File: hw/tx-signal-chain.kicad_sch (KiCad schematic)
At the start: 29 parts, among them J501 Conn_Coaxial_Power, K501 TQ2-5V, Q501 IRFP250NPBF, Q502 2N7002AKRA-QZ, T501 1t (coax center feedthru) : 8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, U501 UCC27511ADBV

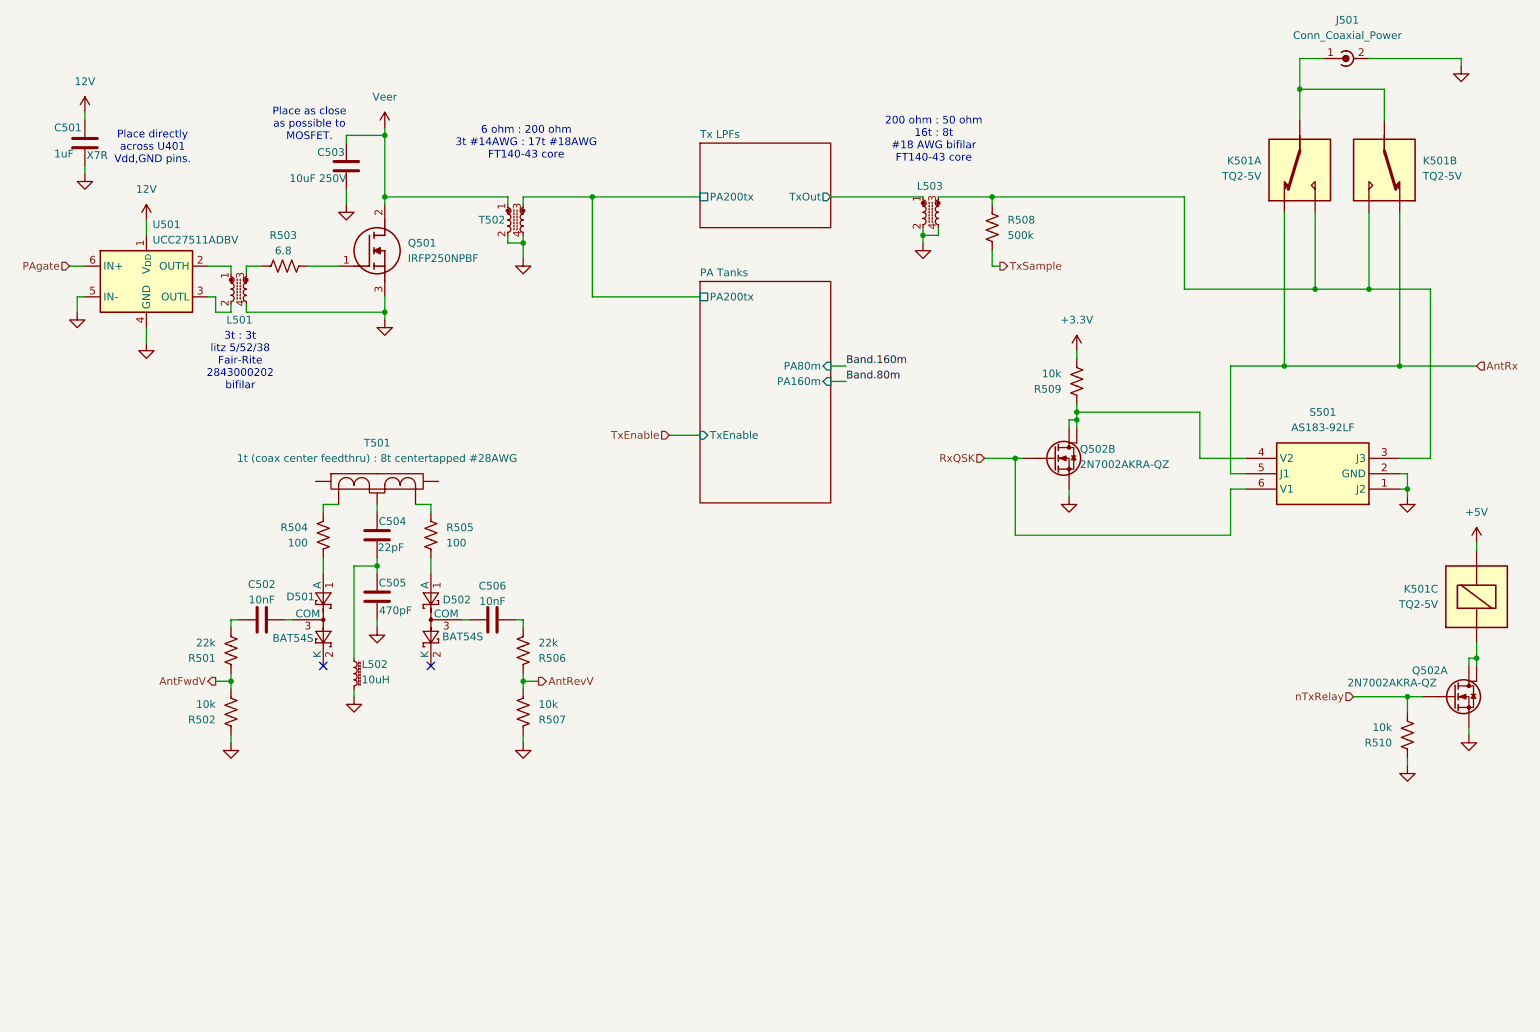
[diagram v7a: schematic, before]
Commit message: Removed USB data, SD card. Added USB-PD (not complete yet). Added SPI display.
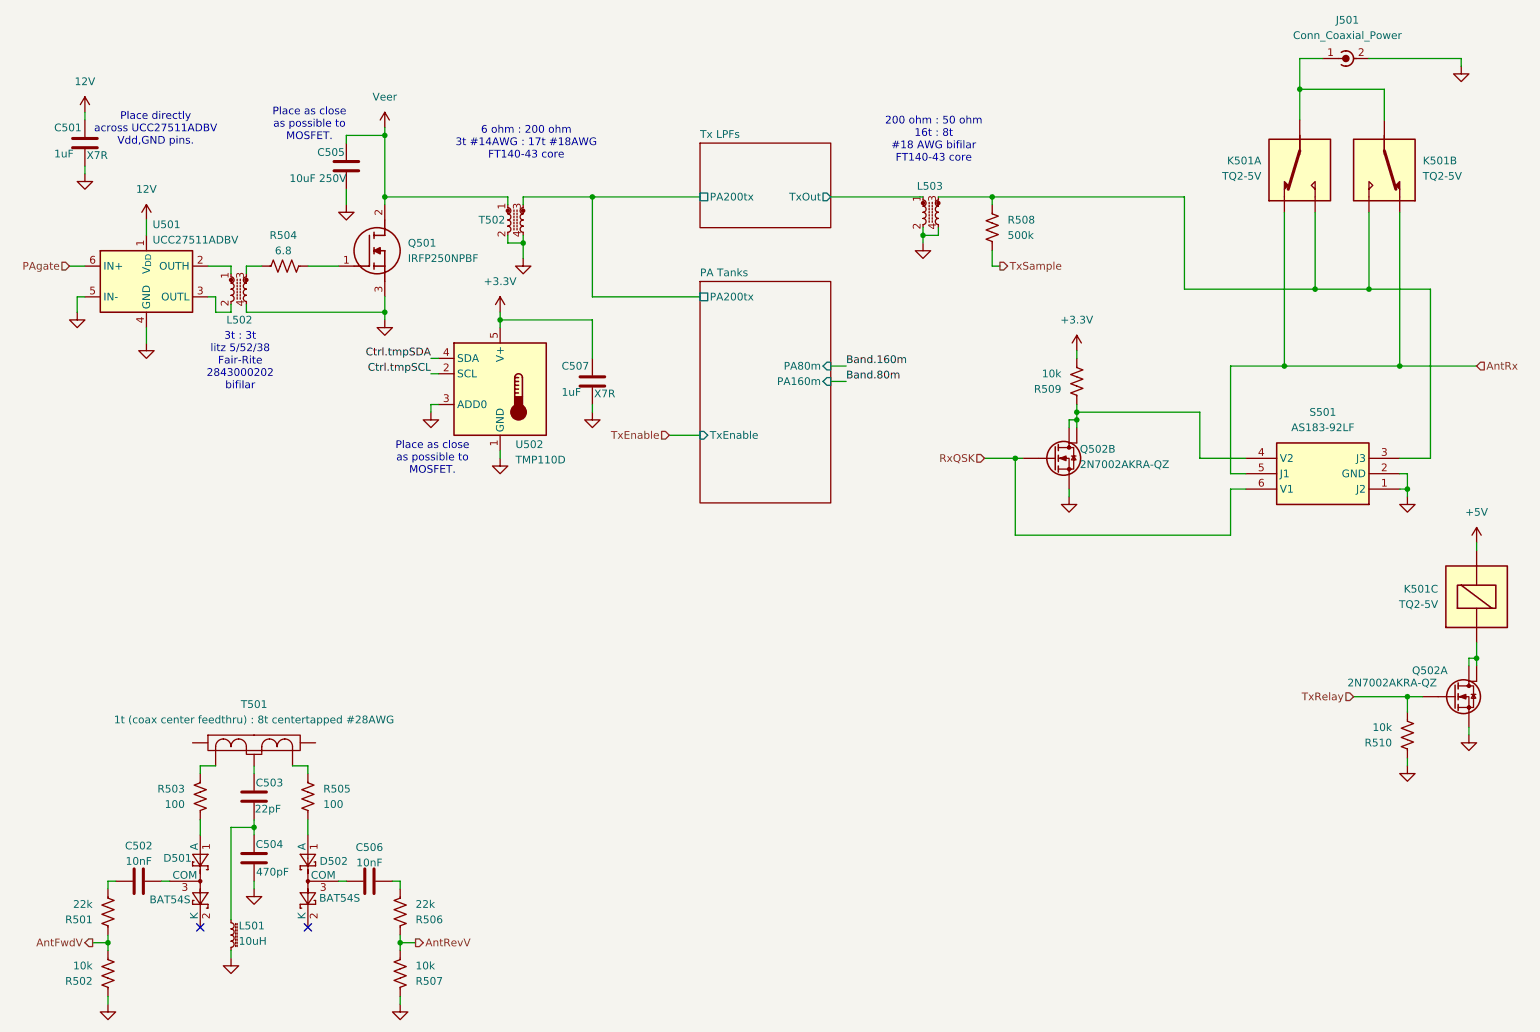
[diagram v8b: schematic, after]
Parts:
- added C507: 1uF, Capacitor_SMD:C_0805_2012Metric, symbol Device:C
- added U502: TMP110D, Package_SON:Texas_X2SON-5_0.8x0.8mm_P0.48mm, symbol Sensor_Temperature:TMP110D
- renumbered C504 to C503, C505 to C504, C503 to C505, L502 to L501, L501 to L502, R504 to R503, R503 to R504
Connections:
- net +3.3V: now also C507.1, U502.5 (V+)
- net GND: now also C507.2, U502.1 (GND), U502.3 (ADD0)
- net nTxRelay renamed TxRelay
- new net Ctrl.tmpSCL: U502.2 (SCL)
- new net Ctrl.tmpSDA: U502.4 (SDA)
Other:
- note added: "Place directly across UCC27511ADBV Vdd,GND pins."
- note removed: "Place directly across U401 Vdd,GND pins."
- moved on the sheet: C502, C503, C504, C506, D501, D502, L501, R501, R502, R503, R505, R506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
